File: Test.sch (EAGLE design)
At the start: 9 parts

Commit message: [add]値
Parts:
- removed R4: (no value), resistor-power:RAC01
- C1: value (none) -> 0.01u
- C2, C4: value (none) -> 0.1u
- C3: value (none) -> 33p
- R1, R2, R3: value (none) -> 200k
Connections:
- removed net N$5: C4.1, R4.1, U$1.VDD
- net +5V: now also C4.1, U$1.VDD; no longer R4.2
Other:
- moved on the sheet: R2
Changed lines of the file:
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@@
 </classes>
 <parts>
-<part name="C1" library="capacitor-wima" library_urn="urn:adsk.eagle:library:116" deviceset="C" device="2.5/2" package3d_urn="urn:adsk.eagle:package:5415/1"/>
-<part name="C2" library="capacitor-wima" library_urn="urn:adsk.eagle:library:116" deviceset="C" device="2.5/2" package3d_urn="urn:adsk.eagle:package:5415/1"/>
-<part name="C3" library="capacitor-wima" library_urn="urn:adsk.eagle:library:116" deviceset="C" device="2.5/2" package3d_urn="urn:adsk.eagle:package:5415/1"/>
-<part name="R1" library="resistor-power" library_urn="urn:adsk.eagle:library:344" deviceset="R" device="AC01" package3d_urn="urn:adsk.eagle:package:25124/1"/>
-<part name="R2" library="resistor-power" library_urn="urn:adsk.eagle:library:344" deviceset="R" device="AC01" package3d_urn="urn:adsk.eagle:package:25124/1"/>
-<part name="R3" library="resistor-power" library_urn="urn:adsk.eagle:library:344" deviceset="R" device="AC01" package3d_urn="urn:adsk.eagle:package:25124/1"/>
+<part name="C1" library="capacitor-wima" library_urn="urn:adsk.eagle:library:116" deviceset="C" device="2.5/2" package3d_urn="urn:adsk.eagle:package:5415/1" value="0.01u"/>
+<part name="C2" library="capacitor-wima" library_urn="urn:adsk.eagle:library:116" deviceset="C" device="2.5/2" package3d_urn="urn:adsk.eagle:package:5415/1" value="0.1u"/>
+<part name="C3" library="capacitor-wima" library_urn="urn:adsk.eagle:library:116" deviceset="C" device="2.5/2" package3d_urn="urn:adsk.eagle:package:5415/1" value="33p"/>
+<part name="R1" library="resistor-power" library_urn="urn:adsk.eagle:library:344" deviceset="R" device="AC01" package3d_urn="urn:adsk.eagle:package:25124/1" value="200k"/>
+<part name="R2" library="resistor-power" library_urn="urn:adsk.eagle:library:344" deviceset="R" device="AC01" package3d_urn="urn:adsk.eagle:package:25124/1" value="200k"/>
+<part name="R3" library="resistor-power" library_urn="urn:adsk.eagle:library:344" deviceset="R" device="AC01" package3d_urn="urn:adsk.eagle:package:25124/1" value="200k"/>
 <part name="P+2" library="supply1" library_urn="urn:adsk.eagle:library:371" deviceset="+5V" device=""/>
 <part name="GND2" library="supply1" library_urn="urn:adsk.eagle:library:371" deviceset="GND" device=""/>
 <part name="GND3" library="supply1" library_urn="urn:adsk.eagle:library:371" deviceset="GND" device=""/>
 <part name="GND4" library="supply1" library_urn="urn:adsk.eagle:library:371" deviceset="GND" device=""/>
-<part name="C4" library="capacitor-wima" library_urn="urn:adsk.eagle:library:116" deviceset="C" device="2.5/2" package3d_urn="urn:adsk.eagle:package:5415/1"/>
-<part name="R4" library="resistor-power" library_urn="urn:adsk.eagle:library:344" deviceset="R" device="AC01" package3d_urn="urn:adsk.eagle:package:25124/1"/>
+<part name="C4" library="capacitor-wima" library_urn="urn:adsk.eagle:library:116" deviceset="C" device="2.5/2" package3d_urn="urn:adsk.eagle:package:5415/1" value="0.1u"/>
 <part name="P+3" library="supply1" library_urn="urn:adsk.eagle:library:371" deviceset="+5V" device=""/>
 <part name="GND5" library="supply1" library_urn="urn:adsk.eagle:library:371" deviceset="GND" device=""/>
@@
 <attribute name="VALUE" x="24.13" y="-28.321" size="1.778" layer="96"/>
 </instance>
-<instance part="R2" gate="G$1" x="27.94" y="-30.48" smashed="yes">
-<attribute name="NAME" x="24.13" y="-29.1084" size="1.778" layer="95"/>
-<attribute name="VALUE" x="24.13" y="-33.401" size="1.778" layer="96"/>
+<instance part="R2" gate="G$1" x="27.94" y="-33.02" smashed="yes">
+<attribute name="NAME" x="24.13" y="-31.6484" size="1.778" layer="95"/>
+<attribute name="VALUE" x="24.13" y="-35.941" size="1.778" layer="96"/>
 </instance>
 <instance part="R3" gate="G$1" x="30.48" y="17.78" smashed="yes" rot="R90">
@@
 <attribute name="VALUE" x="-21.336" y="10.541" size="1.778" layer="96"/>
 </instance>
-<instance part="R4" gate="G$1" x="-22.86" y="25.4" smashed="yes" rot="R90">
-<attribute name="NAME" x="-24.2316" y="21.59" size="1.778" layer="95" rot="R90"/>
-<attribute name="VALUE" x="-19.939" y="21.59" size="1.778" layer="96" rot="R90"/>
-</instance>
-<instance part="P+3" gate="1" x="-22.86" y="33.02" smashed="yes">
-<attribute name="VALUE" x="-25.4" y="27.94" size="1.778" layer="96" rot="R90"/>
+<instance part="P+3" gate="1" x="-22.86" y="27.94" smashed="yes">
+<attribute name="VALUE" x="-25.4" y="22.86" size="1.778" layer="96" rot="R90"/>
 </instance>
 <instance part="GND5" gate="1" x="-22.86" y="7.62" smashed="yes">
@@
 </segment>
 <segment>
+<pinref part="C4" gate="G$1" pin="1"/>
+<wire x1="-22.86" y1="25.4" x2="-22.86" y2="17.78" width="0.1524" layer="91"/>
+<wire x1="-15.24" y1="7.62" x2="-15.24" y2="17.78" width="0.1524" layer="91"/>
+<wire x1="-15.24" y1="17.78" x2="-22.86" y2="17.78" width="0.1524" layer="91"/>
+<junction x="-22.86" y="17.78"/>
+<pinref part="U$1" gate="G$1" pin="VDD"/>
 <pinref part="P+3" gate="1" pin="+5V"/>
-<pinref part="R4" gate="G$1" pin="2"/>
 </segment>
 </net>
@@
 <pinref part="R2" gate="G$1" pin="1"/>
 <pinref part="C1" gate="G$1" pin="2"/>
-<wire x1="22.86" y1="-30.48" x2="20.32" y2="-30.48" width="0.1524" layer="91"/>
-<wire x1="20.32" y1="-30.48" x2="20.32" y2="-25.4" width="0.1524" layer="91"/>
+<wire x1="22.86" y1="-33.02" x2="20.32" y2="-33.02" width="0.1524" layer="91"/>
+<wire x1="20.32" y1="-33.02" x2="20.32" y2="-25.4" width="0.1524" layer="91"/>
 <pinref part="R1" gate="G$1" pin="1"/>
 <wire x1="20.32" y1="-25.4" x2="20.32" y2="-20.32" width="0.1524" layer="91"/>
@@
 </segment>
 </net>
-<net name="N$5" class="0">
-<segment>
-<pinref part="C4" gate="G$1" pin="1"/>
-<pinref part="R4" gate="G$1" pin="1"/>
-<wire x1="-22.86" y1="20.32" x2="-22.86" y2="17.78" width="0.1524" layer="91"/>
-<wire x1="-15.24" y1="7.62" x2="-15.24" y2="17.78" width="0.1524" layer="91"/>
-<wire x1="-15.24" y1="17.78" x2="-22.86" y2="17.78" width="0.1524" layer="91"/>
-<junction x="-22.86" y="17.78"/>
-<pinref part="U$1" gate="G$1" pin="VDD"/>
-</segment>
-</net>

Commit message: [add]LM3914
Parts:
- added R4, R5: (no value), resistor-power:RAC01
- added U$2: LB10, SpectralAnalyzer:LB10
- added U$3: LM3914, SpectralAnalyzer:LM3914
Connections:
- new net +12V: U$3.MODE_SELECT, U$3.V+
- new net N$10: U$2.C1, U$3.LED.NO.2
- new net N$11: U$2.C2, U$3.LED.NO.3
- new net N$12: U$2.C3, U$3.LED.NO.4
- new net N$13: U$2.C4, U$3.LED.NO.5
- new net N$14: U$2.C5, U$3.LED.NO.6
- new net N$15: U$2.C6, U$3.LED.NO.7
- new net N$16: U$2.C7, U$3.LED.NO.8
- new net N$17: U$2.C8, U$3.LED.NO.9
- new net N$18: U$2.C9, U$3.LED.NO.10
- new net N$19: R4.1, R5.2, U$3.REFERENCE_ADJUST
- new net N$21: U$3.SIGNAL_INPUT
- new net N$22: R4.2, U$3.DIVIDER(HIGH_END), U$3.REFERENCE_OUTPUT
- new net N$5: U$1.OUT
- new net N$7: U$1.STROBE
- new net N$8: U$1.RESET
- new net N$9: U$2.C, U$3.LED.NO.1
- net +5V: now also U$2.A, U$2.A1, U$2.A2, U$2.A3, U$2.A4, U$2.A5, U$2.A6, U$2.A7, U$2.A8, U$2.A9
- net GND: now also R5.1, U$3.DIVIDER(LOW_END), U$3.V-
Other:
- note added: "DC_Out"
- note added: "Reset"
- note added: "SIGNAL1"
- note added: "Strobe"

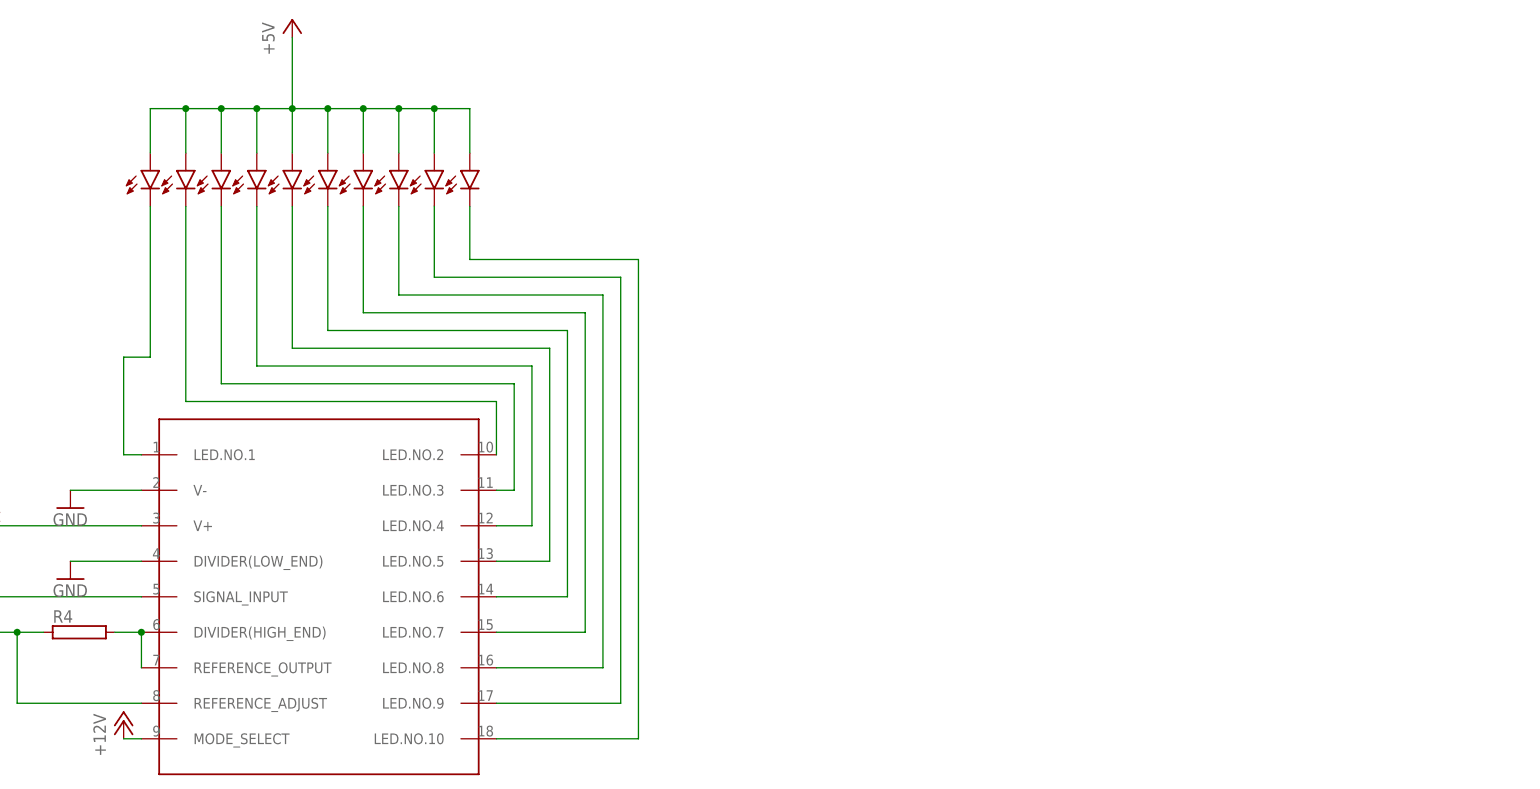
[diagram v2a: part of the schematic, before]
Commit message: [add]LM3914にこめ
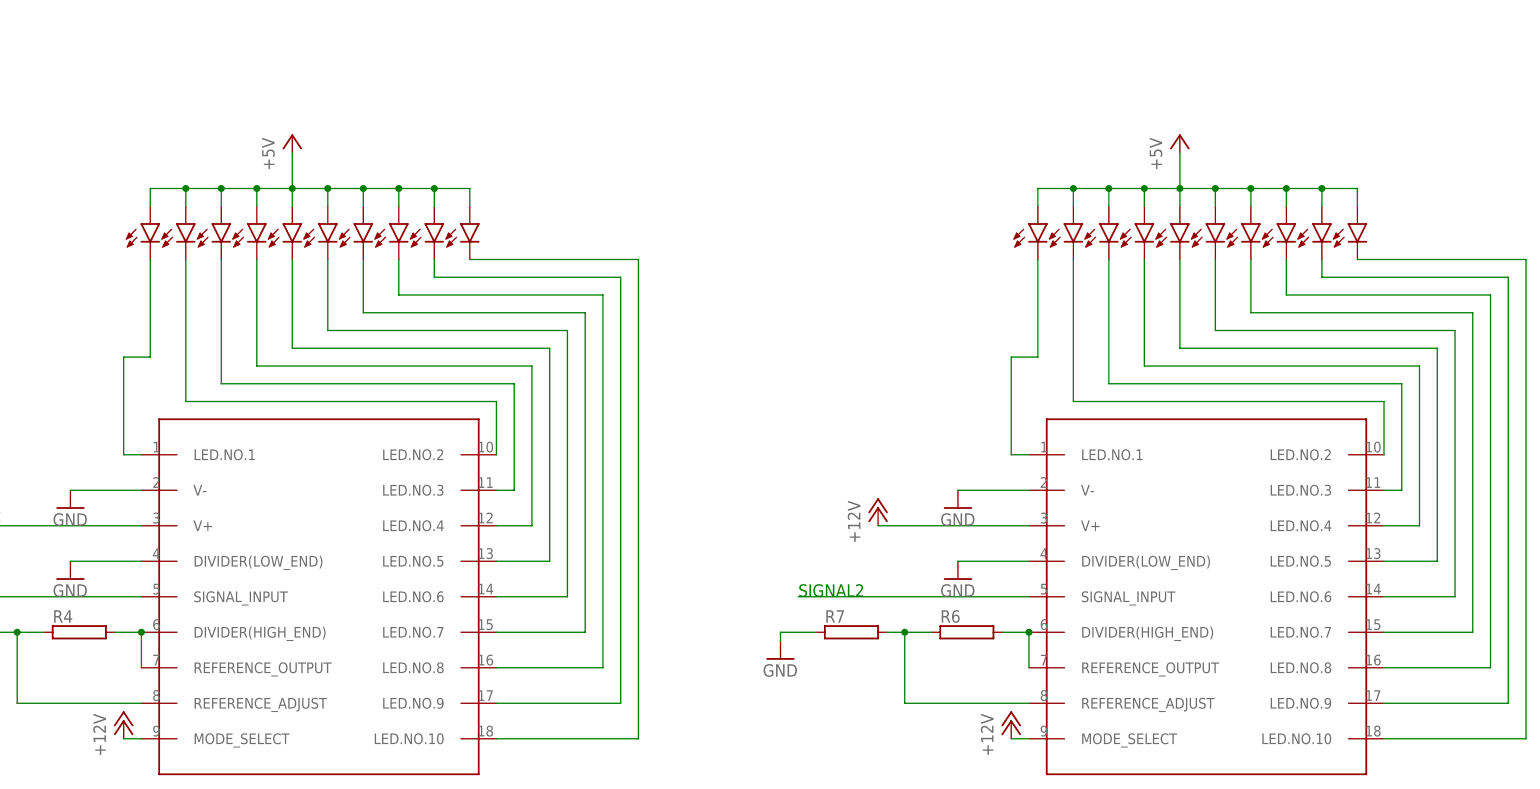
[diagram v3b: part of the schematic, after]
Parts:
- added R6, R7: (no value), resistor-power:RAC01
- added U$4: LB10, SpectralAnalyzer:LB10
- added U$5: LM3914, SpectralAnalyzer:LM3914
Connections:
- new net N$20: U$4.C, U$5.LED.NO.1
- new net N$23: U$4.C1, U$5.LED.NO.2
- new net N$24: U$4.C2, U$5.LED.NO.3
- new net N$25: U$4.C3, U$5.LED.NO.4
- new net N$26: U$4.C4, U$5.LED.NO.5
- new net N$27: U$4.C5, U$5.LED.NO.6
- new net N$28: U$4.C6, U$5.LED.NO.7
- new net N$29: U$4.C7, U$5.LED.NO.8
- new net N$30: U$4.C8, U$5.LED.NO.9
- new net N$31: U$4.C9, U$5.LED.NO.10
- new net N$32: U$5.SIGNAL_INPUT
- new net N$33: R6.2, U$5.DIVIDER(HIGH_END), U$5.REFERENCE_OUTPUT
- new net N$34: R6.1, R7.2, U$5.REFERENCE_ADJUST
- net +12V: now also U$5.MODE_SELECT, U$5.V+
- net +5V: now also U$4.A, U$4.A1, U$4.A2, U$4.A3, U$4.A4, U$4.A5, U$4.A6, U$4.A7, U$4.A8, U$4.A9
- net GND: now also R7.1, U$5.DIVIDER(LOW_END), U$5.V-
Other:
- note added: "SIGNAL2"

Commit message: [add]esp32
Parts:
- added U1: ESP-WROOM-32, SpectralAnalyzer:ESP-WROOM-32
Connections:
- new net N$35: U1.SENSOR_VN
- new net N$36: U1.IO34
- new net N$37: U1.IO35
- new net N$38: U1.IO12
- new net N$39: U1.GND@15
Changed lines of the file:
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@@
 <setting verticaltext="up"/>
 </settings>
-<grid distance="0.05" unitdist="inch" unit="inch" style="lines" multiple="1" display="yes" altdistance="0.01" altunitdist="inch" altunit="inch"/>
+<grid distance="0.1" unitdist="inch" unit="inch" style="lines" multiple="1" display="no" altdistance="0.01" altunitdist="inch" altunit="inch"/>
 <layers>
 <layer number="1" name="Top" color="4" fill="1" visible="no" active="no"/>
@@
 <part name="P+7" library="supply1" library_urn="urn:adsk.eagle:library:371" deviceset="+12V" device=""/>
 <part name="P+8" library="supply1" library_urn="urn:adsk.eagle:library:371" deviceset="+12V" device=""/>
+<part name="U1" library="SpectralAnalyzer" library_urn="urn:adsk.eagle:library:7692814" deviceset="ESP-WROOM-32" device="" package3d_urn="urn:adsk.eagle:package:8041332/1"/>
 </parts>
 <sheets>
@@
 <text x="72.39" y="-30.48" size="1.778" layer="91">SIGNAL1</text>
 <text x="199.39" y="-30.48" size="1.778" layer="91">SIGNAL2</text>
+<text x="-35.56" y="-127" size="1.778" layer="91">Reset</text>
+<text x="-35.56" y="-129.54" size="1.778" layer="91">Strobe</text>
+<text x="-35.56" y="-132.08" size="1.778" layer="91">DC_Out</text>
+<text x="-38.1" y="-149.86" size="1.778" layer="91">SIGNAL1</text>
+<text x="-12.7" y="-172.72" size="1.778" layer="91" rot="R90">SIGNAL2</text>
 </plain>
 <instances>
@@
 <instance part="P+8" gate="1" x="229.87" y="-48.26" smashed="yes">
 <attribute name="VALUE" x="227.33" y="-53.34" size="1.778" layer="96" rot="R90"/>
+</instance>
+<instance part="U1" gate="G$1" x="-7.62" y="-119.38" smashed="yes">
+<attribute name="NAME" x="-20.32" y="-101.346" size="1.778" layer="95"/>
+<attribute name="VALUE" x="-20.32" y="-106.934" size="1.778" layer="96" align="top-left"/>
 </instance>
 </instances>
@@
 </segment>
 </net>
+<net name="N$35" class="0">
+<segment>
+<pinref part="U1" gate="G$1" pin="SENSOR_VN"/>
+<wire x1="-25.4" y1="-127" x2="-35.56" y2="-127" width="0.1524" layer="91"/>
+</segment>
+</net>
+<net name="N$36" class="0">
+<segment>
+<pinref part="U1" gate="G$1" pin="IO34"/>
+<wire x1="-25.4" y1="-129.54" x2="-35.56" y2="-129.54" width="0.1524" layer="91"/>
+</segment>
+</net>
+<net name="N$37" class="0">
+<segment>
+<pinref part="U1" gate="G$1" pin="IO35"/>
+<wire x1="-25.4" y1="-132.08" x2="-35.56" y2="-132.08" width="0.1524" layer="91"/>
+</segment>
+</net>
+<net name="N$38" class="0">
+<segment>
+<pinref part="U1" gate="G$1" pin="IO12"/>
+<wire x1="-25.4" y1="-149.86" x2="-35.56" y2="-149.86" width="0.1524" layer="91"/>
+</segment>
+</net>
+<net name="N$39" class="0">
+<segment>
+<pinref part="U1" gate="G$1" pin="GND@15"/>
+<wire x1="-12.7" y1="-160.02" x2="-12.7" y2="-172.72" width="0.1524" layer="91"/>
+</segment>
+</net>

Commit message: [fix]手直し
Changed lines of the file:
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@@
 <text x="-35.56" y="-127" size="1.778" layer="91">Reset</text>
 <text x="-35.56" y="-129.54" size="1.778" layer="91">Strobe</text>
-<text x="-35.56" y="-132.08" size="1.778" layer="91">DC_Out</text>
-<text x="-38.1" y="-149.86" size="1.778" layer="91">SIGNAL1</text>
-<text x="-12.7" y="-172.72" size="1.778" layer="91" rot="R90">SIGNAL2</text>
 </plain>
 <instances>
